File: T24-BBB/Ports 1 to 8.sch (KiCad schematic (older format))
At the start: 42 parts, among them J1 Port 1, J2 Port 2, J3 Port 3, J4 Port 4, J5 Port 5, J6 Port 6, J7 Port 7, J8 Port 8, U1 74HC245D

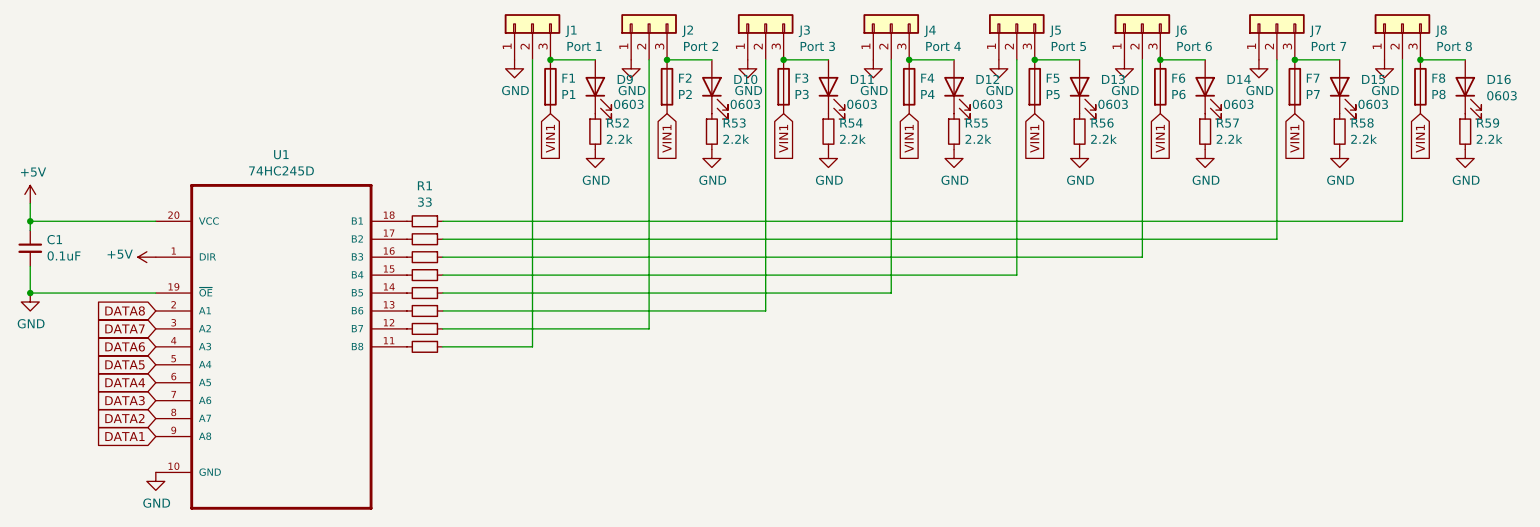
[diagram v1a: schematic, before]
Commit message: Bump to 0.7b
Changed DMX connector. Tweaks.
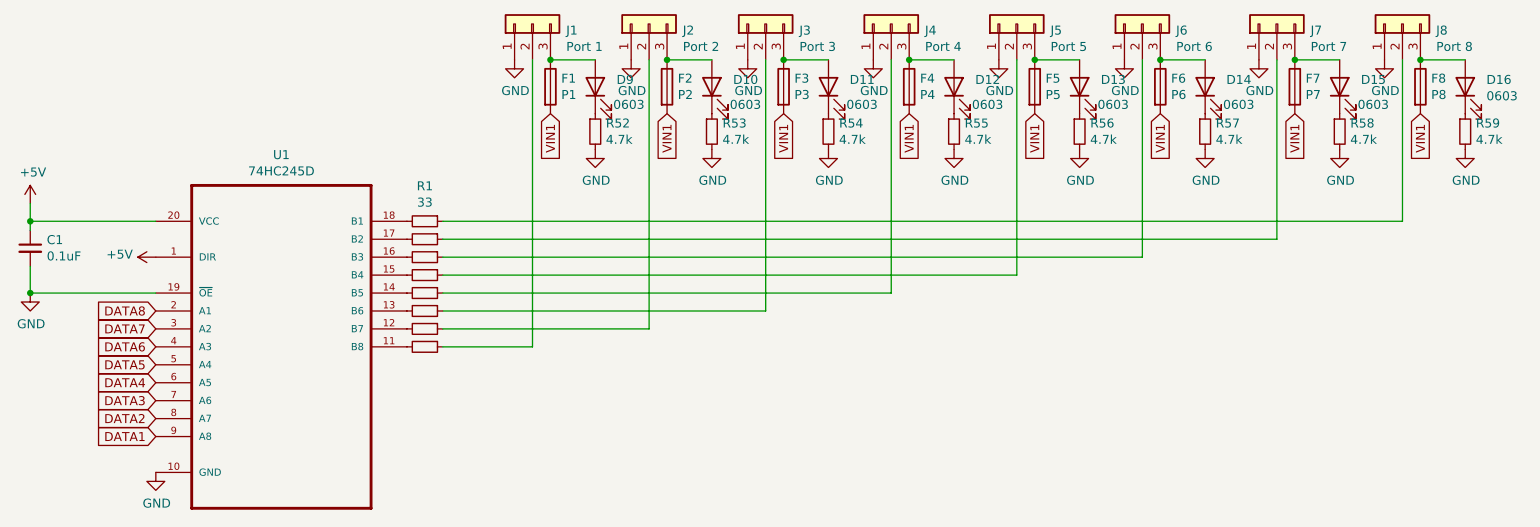
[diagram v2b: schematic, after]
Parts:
- J1, J2, J3, J4, J5, J6, J7, J8: footprint 3544again:TimPheonix -> Connector_Phoenix_MC:PhoenixContact_MCV_1,5_3-G-3.5_1x03_P3.50mm_Vertical
- R52, R53, R54, R55, R56, R57, R58, R59: value 2.2k -> 4.7k; Description C17520 -> C17673
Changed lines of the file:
@@
 Title "T24"
 Date "2021-03-14"
-Rev "0.7a"
+Rev "0.7b"
 Comp "Lights On Windermere Avenue"
 Comment1 ""
@@
 F 0 "J1" V 3714 762 50  0000 R CNN
 F 1 "Port 1" V 3623 762 50  0000 R CNN
-F 2 "3544again:TimPheonix" H 3750 950 50  0001 C CNN
+F 2 "Connector_Phoenix_MC:PhoenixContact_MCV_1,5_3-G-3.5_1x03_P3.50mm_Vertical" H 3750 950 50  0001 C CNN
 F 3 "~" H 3750 950 50  0001 C CNN
 	1    3750 950
@@
 F 0 "J2" V 4364 762 50  0000 R CNN
 F 1 "Port 2" V 4273 762 50  0000 R CNN
-F 2 "3544again:TimPheonix" H 4400 950 50  0001 C CNN
+F 2 "Connector_Phoenix_MC:PhoenixContact_MCV_1,5_3-G-3.5_1x03_P3.50mm_Vertical" H 4400 950 50  0001 C CNN
 F 3 "~" H 4400 950 50  0001 C CNN
 	1    4400 950
@@
 F 0 "J3" V 5014 762 50  0000 R CNN
 F 1 "Port 3" V 4923 762 50  0000 R CNN
-F 2 "3544again:TimPheonix" H 5050 950 50  0001 C CNN
+F 2 "Connector_Phoenix_MC:PhoenixContact_MCV_1,5_3-G-3.5_1x03_P3.50mm_Vertical" H 5050 950 50  0001 C CNN
 F 3 "~" H 5050 950 50  0001 C CNN
 	1    5050 950
@@
 F 0 "J4" V 5714 762 50  0000 R CNN
 F 1 "Port 4" V 5623 762 50  0000 R CNN
-F 2 "3544again:TimPheonix" H 5750 950 50  0001 C CNN
+F 2 "Connector_Phoenix_MC:PhoenixContact_MCV_1,5_3-G-3.5_1x03_P3.50mm_Vertical" H 5750 950 50  0001 C CNN
 F 3 "~" H 5750 950 50  0001 C CNN
 	1    5750 950
@@
 F 0 "J5" V 6414 762 50  0000 R CNN
 F 1 "Port 5" V 6323 762 50  0000 R CNN
-F 2 "3544again:TimPheonix" H 6450 950 50  0001 C CNN
+F 2 "Connector_Phoenix_MC:PhoenixContact_MCV_1,5_3-G-3.5_1x03_P3.50mm_Vertical" H 6450 950 50  0001 C CNN
 F 3 "~" H 6450 950 50  0001 C CNN
 	1    6450 950
@@
 F 0 "J6" V 7114 762 50  0000 R CNN
 F 1 "Port 6" V 7023 762 50  0000 R CNN
-F 2 "3544again:TimPheonix" H 7150 950 50  0001 C CNN
+F 2 "Connector_Phoenix_MC:PhoenixContact_MCV_1,5_3-G-3.5_1x03_P3.50mm_Vertical" H 7150 950 50  0001 C CNN
 F 3 "~" H 7150 950 50  0001 C CNN
 	1    7150 950
@@
 F 0 "J7" V 7864 762 50  0000 R CNN
 F 1 "Port 7" V 7773 762 50  0000 R CNN
-F 2 "3544again:TimPheonix" H 7900 950 50  0001 C CNN
+F 2 "Connector_Phoenix_MC:PhoenixContact_MCV_1,5_3-G-3.5_1x03_P3.50mm_Vertical" H 7900 950 50  0001 C CNN
 F 3 "~" H 7900 950 50  0001 C CNN
 	1    7900 950
@@
 F 0 "J8" V 8564 762 50  0000 R CNN
 F 1 "Port 8" V 8473 762 50  0000 R CNN
-F 2 "3544again:TimPheonix" H 8600 950 50  0001 C CNN
+F 2 "Connector_Phoenix_MC:PhoenixContact_MCV_1,5_3-G-3.5_1x03_P3.50mm_Vertical" H 8600 950 50  0001 C CNN
 F 3 "~" H 8600 950 50  0001 C CNN
 	1    8600 950
@@
 P 8950 1550
 F 0 "R59" H 9009 1596 50  0000 L CNN
-F 1 "2.2k" H 9009 1505 50  0000 L CNN
+F 1 "4.7k" H 9009 1505 50  0000 L CNN
 F 2 "3544again:R_0805_2012Metric" H 8950 1550 50  0001 C CNN
 F 3 "https://datasheet.lcsc.com/szlcsc/Uniroyal-Elec-0805W8F2201T5E_C17520.pdf" H 8950 1550 50  0001 C CNN
-F 4 "C17520" H 8950 1550 50  0001 C CNN "Description"
+F 4 "C17673" H 8950 1550 50  0001 C CNN "Description"
 	1    8950 1550
 	1    0    0    -1
@@
 P 8250 1550
 F 0 "R58" H 8309 1596 50  0000 L CNN
-F 1 "2.2k" H 8309 1505 50  0000 L CNN
+F 1 "4.7k" H 8309 1505 50  0000 L CNN
 F 2 "3544again:R_0805_2012Metric" H 8250 1550 50  0001 C CNN
 F 3 "https://datasheet.lcsc.com/szlcsc/Uniroyal-Elec-0805W8F2201T5E_C17520.pdf" H 8250 1550 50  0001 C CNN
-F 4 "C17520" H 8250 1550 50  0001 C CNN "Description"
+F 4 "C17673" H 8250 1550 50  0001 C CNN "Description"
 	1    8250 1550
 	1    0    0    -1
@@
 P 7500 1550
 F 0 "R57" H 7559 1596 50  0000 L CNN
-F 1 "2.2k" H 7559 1505 50  0000 L CNN
+F 1 "4.7k" H 7559 1505 50  0000 L CNN
 F 2 "3544again:R_0805_2012Metric" H 7500 1550 50  0001 C CNN
 F 3 "https://datasheet.lcsc.com/szlcsc/Uniroyal-Elec-0805W8F2201T5E_C17520.pdf" H 7500 1550 50  0001 C CNN
-F 4 "C17520" H 7500 1550 50  0001 C CNN "Description"
+F 4 "C17673" H 7500 1550 50  0001 C CNN "Description"
 	1    7500 1550
 	1    0    0    -1
@@
 P 6800 1550
 F 0 "R56" H 6859 1596 50  0000 L CNN
-F 1 "2.2k" H 6859 1505 50  0000 L CNN
+F 1 "4.7k" H 6859 1505 50  0000 L CNN
 F 2 "3544again:R_0805_2012Metric" H 6800 1550 50  0001 C CNN
 F 3 "https://datasheet.lcsc.com/szlcsc/Uniroyal-Elec-0805W8F2201T5E_C17520.pdf" H 6800 1550 50  0001 C CNN
-F 4 "C17520" H 6800 1550 50  0001 C CNN "Description"
+F 4 "C17673" H 6800 1550 50  0001 C CNN "Description"
 	1    6800 1550
 	1    0    0    -1
@@
 P 6100 1550
 F 0 "R55" H 6159 1596 50  0000 L CNN
-F 1 "2.2k" H 6159 1505 50  0000 L CNN
+F 1 "4.7k" H 6159 1505 50  0000 L CNN
 F 2 "3544again:R_0805_2012Metric" H 6100 1550 50  0001 C CNN
 F 3 "https://datasheet.lcsc.com/szlcsc/Uniroyal-Elec-0805W8F2201T5E_C17520.pdf" H 6100 1550 50  0001 C CNN
-F 4 "C17520" H 6100 1550 50  0001 C CNN "Description"
+F 4 "C17673" H 6100 1550 50  0001 C CNN "Description"
 	1    6100 1550
 	1    0    0    -1
@@
 P 5400 1550
 F 0 "R54" H 5459 1596 50  0000 L CNN
-F 1 "2.2k" H 5459 1505 50  0000 L CNN
+F 1 "4.7k" H 5459 1505 50  0000 L CNN
 F 2 "3544again:R_0805_2012Metric" H 5400 1550 50  0001 C CNN
 F 3 "https://datasheet.lcsc.com/szlcsc/Uniroyal-Elec-0805W8F2201T5E_C17520.pdf" H 5400 1550 50  0001 C CNN
-F 4 "C17520" H 5400 1550 50  0001 C CNN "Description"
+F 4 "C17673" H 5400 1550 50  0001 C CNN "Description"
 	1    5400 1550
 	1    0    0    -1
@@
 P 4750 1550
 F 0 "R53" H 4809 1596 50  0000 L CNN
-F 1 "2.2k" H 4809 1505 50  0000 L CNN
+F 1 "4.7k" H 4809 1505 50  0000 L CNN
 F 2 "3544again:R_0805_2012Metric" H 4750 1550 50  0001 C CNN
 F 3 "https://datasheet.lcsc.com/szlcsc/Uniroyal-Elec-0805W8F2201T5E_C17520.pdf" H 4750 1550 50  0001 C CNN
-F 4 "C17520" H 4750 1550 50  0001 C CNN "Description"
+F 4 "C17673" H 4750 1550 50  0001 C CNN "Description"
 	1    4750 1550
 	1    0    0    -1
@@
 P 4100 1550
 F 0 "R52" H 4159 1596 50  0000 L CNN
-F 1 "2.2k" H 4159 1505 50  0000 L CNN
+F 1 "4.7k" H 4159 1505 50  0000 L CNN
 F 2 "3544again:R_0805_2012Metric" H 4100 1550 50  0001 C CNN
 F 3 "https://datasheet.lcsc.com/szlcsc/Uniroyal-Elec-0805W8F2201T5E_C17520.pdf" H 4100 1550 50  0001 C CNN
-F 4 "C17520" H 4100 1550 50  0001 C CNN "Description"
+F 4 "C17673" H 4100 1550 50  0001 C CNN "Description"
 	1    4100 1550
 	1    0    0    -1
